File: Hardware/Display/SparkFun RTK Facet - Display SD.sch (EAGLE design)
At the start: 30 parts, among them J1 FPC_12_0.5MM_BACKFLIP, J2 MICRO-SD-PUSH-PUSH-EXT-PIN, J3 FPC_12_0.5MM_BACKFLIP, U13 LIS2DH12

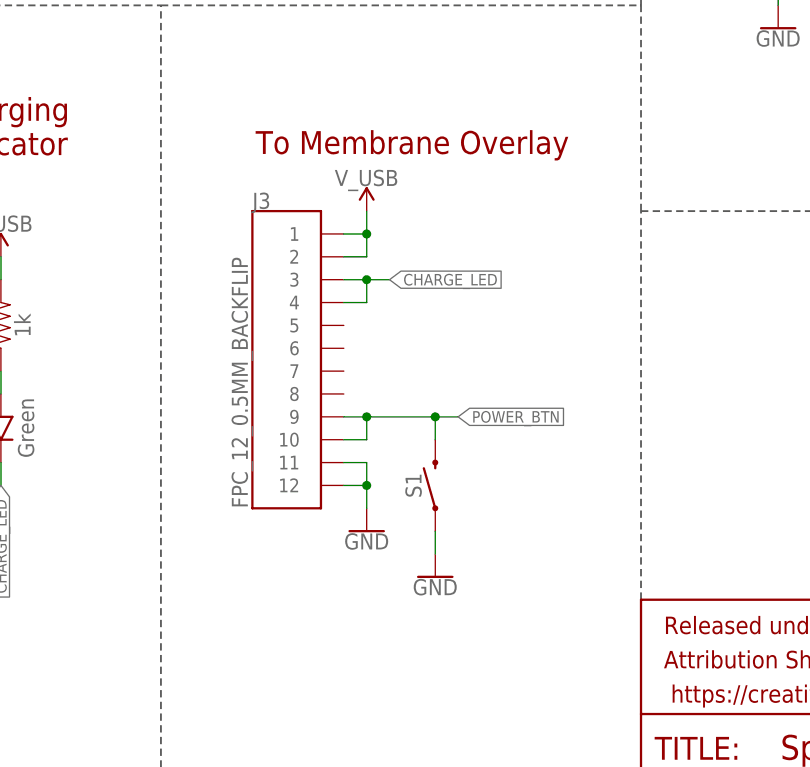
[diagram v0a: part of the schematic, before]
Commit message: Move to LIF overlay connector.
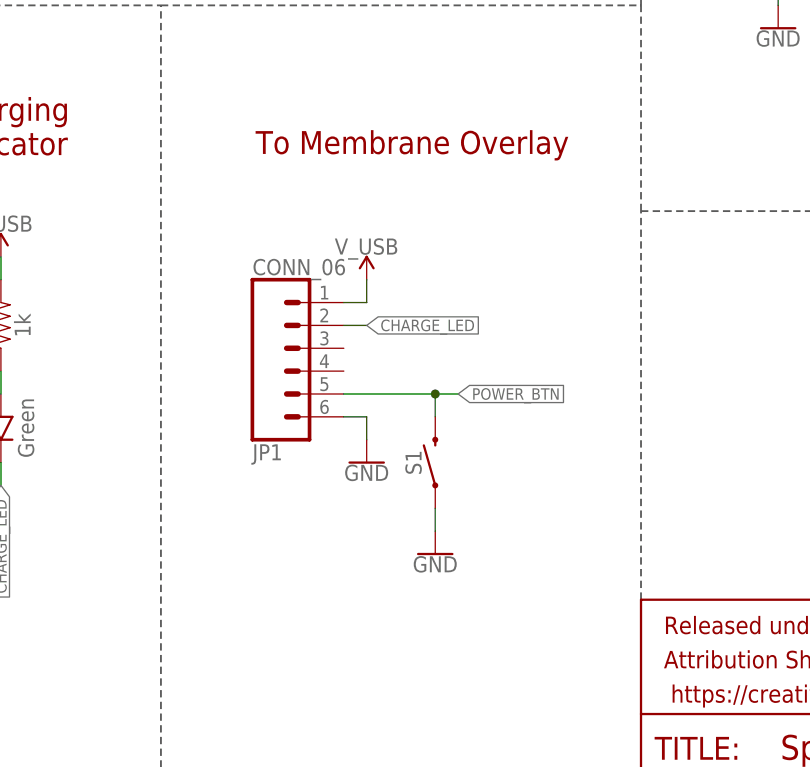
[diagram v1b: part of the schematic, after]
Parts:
- removed J3: FPC_12_0.5MM_BACKFLIP, RTK Facet:FPC_12_0.5MM_BACKFLIP
- added JP1: CONN_06, 1mm Pitch Connector:CONN_06
- LOGO5: value SFE_LOGO_NAME_FLAME.1_INCH -> SFE_LOGO_NAME_FLAME8_MM; device SparkFun-Aesthetics:SFE_LOGO_NAME_FLAME.1_INCH -> SparkFun-Aesthetics:SFE_LOGO_NAME_FLAME8_MM
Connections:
- net CHARGE_LED: now also JP1.2; no longer J3.3, J3.4
- net GND: now also JP1.6; no longer J3.11, J3.12
- net POWER_BTN: now also JP1.5; no longer J3.10, J3.9
- net V_USB: now also JP1.1; no longer J3.1, J3.2
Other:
- moved on the sheet: S1

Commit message: v15 panel files. Add tCream to LIF.
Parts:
- JP1: value CONN_06 -> (none); device 1mm Pitch Connector:CONN_06 -> SparkFun-Connectors:CONN_061MM-LIF
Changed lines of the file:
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@@
 <grid distance="0.1" unitdist="inch" unit="inch" style="lines" multiple="1" display="no" altdistance="0.01" altunitdist="inch" altunit="inch"/>
 <layers>
-<layer number="1" name="Top" color="4" fill="1" visible="yes" active="no"/>
-<layer number="2" name="Route2" color="1" fill="3" visible="yes" active="no"/>
-<layer number="3" name="Route3" color="4" fill="3" visible="yes" active="no"/>
-<layer number="4" name="Route4" color="1" fill="4" visible="yes" active="no"/>
-<layer number="5" name="Route5" color="4" fill="4" visible="yes" active="no"/>
-<layer number="6" name="Route6" color="1" fill="8" visible="yes" active="no"/>
-<layer number="7" name="Route7" color="4" fill="8" visible="yes" active="no"/>
-<layer number="8" name="Route8" color="1" fill="2" visible="yes" active="no"/>
-<layer number="9" name="Route9" color="4" fill="2" visible="yes" active="no"/>
-<layer number="10" name="Route10" color="1" fill="7" visible="yes" active="no"/>
-<layer number="11" name="Route11" color="4" fill="7" visible="yes" active="no"/>
-<layer number="12" name="Route12" color="1" fill="5" visible="yes" active="no"/>
-<layer number="13" name="Route13" color="4" fill="5" visible="yes" active="no"/>
-<layer number="14" name="Route14" color="1" fill="6" visible="yes" active="no"/>
-<layer number="15" name="Route15" color="4" fill="6" visible="yes" active="no"/>
-<layer number="16" name="Bottom" color="1" fill="1" visible="yes" active="no"/>
-<layer number="17" name="Pads" color="2" fill="1" visible="yes" active="no"/>
-<layer number="18" name="Vias" color="2" fill="1" visible="yes" active="no"/>
-<layer number="19" name="Unrouted" color="6" fill="1" visible="yes" active="no"/>
-<layer number="20" name="Dimension" color="24" fill="1" visible="yes" active="no"/>
-<layer number="21" name="tPlace" color="16" fill="1" visible="yes" active="no"/>
-<layer number="22" name="bPlace" color="14" fill="1" visible="yes" active="no"/>
-<layer number="23" name="tOrigins" color="15" fill="1" visible="yes" active="no"/>
-<layer number="24" name="bOrigins" color="15" fill="1" visible="yes" active="no"/>
-<layer number="25" name="tNames" color="7" fill="1" visible="yes" active="no"/>
-<layer number="26" name="bNames" color="7" fill="1" visible="yes" active="no"/>
-<layer number="27" name="tValues" color="7" fill="1" visible="yes" active="no"/>
-<layer number="28" name="bValues" color="7" fill="1" visible="yes" active="no"/>
+<layer number="1" name="Top" color="4" fill="1" visible="no" active="no"/>
+<layer number="2" name="Route2" color="1" fill="3" visible="no" active="no"/>
+<layer number="3" name="Route3" color="4" fill="3" visible="no" active="no"/>
+<layer number="4" name="Route4" color="1" fill="4" visible="no" active="no"/>
+<layer number="5" name="Route5" color="4" fill="4" visible="no" active="no"/>
+<layer number="6" name="Route6" color="1" fill="8" visible="no" active="no"/>
+<layer number="7" name="Route7" color="4" fill="8" visible="no" active="no"/>
+<layer number="8" name="Route8" color="1" fill="2" visible="no" active="no"/>
+<layer number="9" name="Route9" color="4" fill="2" visible="no" active="no"/>
+<layer number="10" name="Route10" color="1" fill="7" visible="no" active="no"/>
+<layer number="11" name="Route11" color="4" fill="7" visible="no" active="no"/>
+<layer number="12" name="Route12" color="1" fill="5" visible="no" active="no"/>
+<layer number="13" name="Route13" color="4" fill="5" visible="no" active="no"/>
+<layer number="14" name="Route14" color="1" fill="6" visible="no" active="no"/>
+<layer number="15" name="Route15" color="4" fill="6" visible="no" active="no"/>
+<layer number="16" name="Bottom" color="1" fill="1" visible="no" active="no"/>
+<layer number="17" name="Pads" color="2" fill="1" visible="no" active="no"/>
+<layer number="18" name="Vias" color="2" fill="1" visible="no" active="no"/>
+<layer number="19" name="Unrouted" color="6" fill="1" visible="no" active="no"/>
+<layer number="20" name="Dimension" color="24" fill="1" visible="no" active="no"/>
+<layer number="21" name="tPlace" color="16" fill="1" visible="no" active="no"/>
+<layer number="22" name="bPlace" color="14" fill="1" visible="no" active="no"/>
+<layer number="23" name="tOrigins" color="15" fill="1" visible="no" active="no"/>
+<layer number="24" name="bOrigins" color="15" fill="1" visible="no" active="no"/>
+<layer number="25" name="tNames" color="7" fill="1" visible="no" active="no"/>
+<layer number="26" name="bNames" color="7" fill="1" visible="no" active="no"/>
+<layer number="27" name="tValues" color="7" fill="1" visible="no" active="no"/>
+<layer number="28" name="bValues" color="7" fill="1" visible="no" active="no"/>
 <layer number="29" name="tStop" color="7" fill="3" visible="no" active="no"/>
 <layer number="30" name="bStop" color="7" fill="6" visible="no" active="no"/>
@@
 <layer number="35" name="tGlue" color="7" fill="4" visible="no" active="no"/>
 <layer number="36" name="bGlue" color="7" fill="5" visible="no" active="no"/>
-<layer number="37" name="tTest" color="7" fill="1" visible="yes" active="no"/>
-<layer number="38" name="bTest" color="7" fill="1" visible="yes" active="no"/>
+<layer number="37" name="tTest" color="7" fill="1" visible="no" active="no"/>
+<layer number="38" name="bTest" color="7" fill="1" visible="no" active="no"/>
 <layer number="39" name="tKeepout" color="4" fill="11" visible="no" active="no"/>
 <layer number="40" name="bKeepout" color="1" fill="11" visible="no" active="no"/>
@@
 <layer number="44" name="Drills" color="7" fill="1" visible="no" active="no"/>
 <layer number="45" name="Holes" color="7" fill="1" visible="no" active="no"/>
-<layer number="46" name="Milling" color="3" fill="1" visible="yes" active="no"/>
-<layer number="47" name="Measures" color="7" fill="1" visible="yes" active="no"/>
-<layer number="48" name="Document" color="7" fill="1" visible="yes" active="no"/>
-<layer number="49" name="Reference" color="7" fill="1" visible="yes" active="no"/>
-<layer number="50" name="dxf" color="7" fill="1" visible="yes" active="no"/>
-<layer number="51" name="tDocu" color="6" fill="1" visible="yes" active="no"/>
-<layer number="52" name="bDocu" color="7" fill="1" visible="yes" active="no"/>
-<layer number="53" name="tGND_GNDA" color="7" fill="1" visible="yes" active="no"/>
-<layer number="54" name="bGND_GNDA" color="7" fill="1" visible="yes" active="no"/>
-<layer number="56" name="wert" color="7" fill="1" visible="yes" active="no"/>
-<layer number="57" name="tCAD" color="7" fill="1" visible="yes" active="no"/>
-<layer number="58" name="bCAD" color="7" fill="1" visible="yes" active="no"/>
-<layer number="59" name="tCarbon" color="7" fill="1" visible="yes" active="no"/>
-<layer number="60" name="bCarbon" color="7" fill="1" visible="yes" active="no"/>
+<layer number="46" name="Milling" color="3" fill="1" visible="no" active="no"/>
+<layer number="47" name="Measures" color="7" fill="1" visible="no" active="no"/>
+<layer number="48" name="Document" color="7" fill="1" visible="no" active="no"/>
+<layer number="49" name="Reference" color="7" fill="1" visible="no" active="no"/>
+<layer number="50" name="dxf" color="7" fill="1" visible="no" active="no"/>
+<layer number="51" name="tDocu" color="6" fill="1" visible="no" active="no"/>
+<layer number="52" name="bDocu" color="7" fill="1" visible="no" active="no"/>
+<layer number="53" name="tGND_GNDA" color="7" fill="1" visible="no" active="no"/>
+<layer number="54" name="bGND_GNDA" color="7" fill="1" visible="no" active="no"/>
+<layer number="56" name="wert" color="7" fill="1" visible="no" active="no"/>
+<layer number="57" name="tCAD" color="7" fill="1" visible="no" active="no"/>
+<layer number="58" name="bCAD" color="7" fill="1" visible="no" active="no"/>
+<layer number="59" name="tCarbon" color="7" fill="1" visible="no" active="no"/>
+<layer number="60" name="bCarbon" color="7" fill="1" visible="no" active="no"/>
 <layer number="88" name="SimResults" color="9" fill="1" visible="yes" active="yes"/>
 <layer number="89" name="SimProbes" color="9" fill="1" visible="yes" active="yes"/>
@@
 <layer number="154" name="FabDoc2" color="7" fill="1" visible="yes" active="yes"/>
 <layer number="155" name="FabDoc3" color="7" fill="1" visible="yes" active="yes"/>
+<layer number="156" name="gesam-Maß" color="7" fill="1" visible="no" active="no"/>
+<layer number="157" name="FaceMchng" color="7" fill="1" visible="no" active="no"/>
+<layer number="158" name="FaceMMeas" color="7" fill="1" visible="no" active="no"/>
+<layer number="159" name="Geh-Bear2" color="7" fill="1" visible="no" active="no"/>
+<layer number="160" name="Topologie" color="7" fill="1" visible="no" active="no"/>
+<layer number="161" name="tomplace2" color="7" fill="1" visible="no" active="no"/>
 <layer number="166" name="AntennaArea" color="7" fill="1" visible="no" active="no"/>
 <layer number="168" name="4mmHeightArea" color="7" fill="1" visible="no" active="no"/>
@@
 <layer number="250" name="Descript" color="7" fill="1" visible="yes" active="yes"/>
 <layer number="251" name="SMDround" color="7" fill="1" visible="yes" active="yes"/>
+<layer number="252" name="BR-BS" color="7" fill="1" visible="no" active="no"/>
 <layer number="253" name="Extra" color="7" fill="1" visible="no" active="no"/>
 <layer number="254" name="cooling" color="7" fill="1" visible="yes" active="yes"/>
@@
 <part name="SUPPLY11" library="SparkFun-PowerSymbols" deviceset="V_USB" device=""/>
 <part name="J2" library="SparkFun-Connectors" deviceset="MICRO-SD" device="-PUSH-PUSH-EXT-PIN"/>
-<part name="JP1" library="1mm Pitch Connector" deviceset="CONN_06" device=""/>
+<part name="JP1" library="SparkFun-Connectors" deviceset="CONN_06" device="1MM-LIF"/>
 <part name="SUPPLY9" library="SparkFun-PowerSymbols" deviceset="V_USB" device=""/>
 <part name="GND7" library="SparkFun-PowerSymbols" deviceset="GND" device=""/>

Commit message: Add I2C addresses to schematics
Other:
- note added: "7-Bit unshifted I²C address: 0x19"
- note added: "7-Bit unshifted I²C address: 0x3D"
- note removed: "7-Bit unshifted I2C address: 0x19"
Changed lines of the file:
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@@
 permanent I2C mode.</text>
 <text x="198.12" y="177.8" size="2.54" layer="94" align="center">microSD</text>
-<text x="200.66" y="86.36" size="1.778" layer="97" align="center">7-Bit unshifted I2C address: 0x19</text>
+<text x="200.66" y="86.36" size="1.778" layer="97" align="center">7-Bit unshifted I²C address: 0x19</text>
 <text x="198.12" y="129.54" size="2.54" layer="94" font="vector" align="center">LIS2DH12 / Accelerometer</text>
 <text x="121.92" y="86.36" size="2.54" layer="94" rot="MR180" align="center">To Membrane Overlay</text>
@@
 Indicator</text>
 <text x="171.196" y="11.43" size="2.54" layer="94" font="vector">N. Seidle</text>
+<text x="114.3" y="106.68" size="1.778" layer="97" align="center">7-Bit unshifted I²C address: 0x3D</text>
 </plain>
 <instances>

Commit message: Add I2C test header to display board - v1.6
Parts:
- added J3: (no value), SparkFun-Connectors:I2C_STANDARD_NO_SILK
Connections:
- net 3.3V: now also J3.2
- net ESP_21/SDA: now also J3.3
- net ESP_22/SCL: now also J3.4
- net GND: now also J3.1

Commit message: Remove silk from around the accel FP for DFM.
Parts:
- U13: value LIS2DH12 -> LIS2DH12NS; device SparkFun-Sensors:LIS2DH12 -> SparkFun-Sensors:LIS2DH12NS
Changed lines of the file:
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@@
 <part name="C7" library="SparkFun-Capacitors" deviceset="1.0UF" device="-0603-16V-10%" value="1.0uF"/>
 <part name="R2" library="SparkFun-Resistors" deviceset="10KOHM" device="-0603-1/10W-1%" value="10k"/>
-<part name="JP3" library="SparkFun-Jumpers" deviceset="JUMPER-SMT_2_NO" device="_SILK" package3d_urn="urn:adsk.eagle:package:39279/1" value=""/>
+<part name="JP3" library="SparkFun-Jumpers" deviceset="JUMPER-SMT_2_NO" device="_SILK" package3d_urn="urn:adsk.eagle:package:39279/1" value="JUMPER-SMT_2_NO_SILK"/>
 <part name="FID3" library="SparkFun-Aesthetics" deviceset="FIDUCIAL" device="1X2"/>
 <part name="FID4" library="SparkFun-Aesthetics" deviceset="FIDUCIAL" device="1X2"/>
@@
 <part name="GND2" library="SparkFun-PowerSymbols" deviceset="GND" device=""/>
 <part name="J1" library="RTK Facet" deviceset="FPC_12_0.5MM" device="_BACKFLIP" value="FPC_12_0.5MM_BACKFLIP"/>
-<part name="U13" library="SparkFun-Sensors" deviceset="LIS2DH12" device=""/>
+<part name="U13" library="SparkFun-Sensors" deviceset="LIS2DH12" device="NS" value="LIS2DH12NS"/>
 <part name="GND4" library="SparkFun-PowerSymbols" deviceset="GND" device=""/>
 <part name="GND1" library="SparkFun-PowerSymbols" deviceset="GND" device=""/>
@@
 <attribute name="VALUE" x="19.558" y="43.434" size="1.778" layer="96" rot="R90"/>
 </instance>
-<instance part="U13" gate="G$1" x="200.66" y="106.68" smashed="yes">
+<instance part="U13" gate="U1" x="200.66" y="106.68" smashed="yes">
 <attribute name="NAME" x="190.5" y="119.634" size="1.778" layer="95"/>
 <attribute name="VALUE" x="190.5" y="94.234" size="1.778" layer="96" rot="MR180" align="top-left"/>
@@
 </segment>
 <segment>
-<pinref part="U13" gate="G$1" pin="GND"/>
+<pinref part="U13" gate="U1" pin="GND"/>
 <pinref part="GND4" gate="1" pin="GND"/>
 <wire x1="187.96" y1="99.06" x2="185.42" y2="99.06" width="0.1524" layer="91"/>
 <wire x1="185.42" y1="99.06" x2="185.42" y2="96.52" width="0.1524" layer="91"/>
-<pinref part="U13" gate="G$1" pin="RES"/>
+<pinref part="U13" gate="U1" pin="RES"/>
 <wire x1="187.96" y1="104.14" x2="185.42" y2="104.14" width="0.1524" layer="91"/>
 <wire x1="185.42" y1="104.14" x2="185.42" y2="99.06" width="0.1524" layer="91"/>
@@
 </segment>
 <segment>
-<pinref part="U13" gate="G$1" pin="VDD_IO"/>
+<pinref part="U13" gate="U1" pin="VDD_IO"/>
 <wire x1="187.96" y1="116.84" x2="185.42" y2="116.84" width="0.1524" layer="91"/>
-<pinref part="U13" gate="G$1" pin="VDD"/>
+<pinref part="U13" gate="U1" pin="VDD"/>
 <wire x1="187.96" y1="114.3" x2="185.42" y2="114.3" width="0.1524" layer="91"/>
 <wire x1="185.42" y1="114.3" x2="185.42" y2="116.84" width="0.1524" layer="91"/>
@@
 </segment>
 <segment>
-<pinref part="U13" gate="G$1" pin="CS"/>
+<pinref part="U13" gate="U1" pin="CS"/>
 <wire x1="213.36" y1="116.84" x2="215.9" y2="116.84" width="0.1524" layer="91"/>
 <wire x1="215.9" y1="116.84" x2="215.9" y2="119.38" width="0.1524" layer="91"/>
 <junction x="215.9" y="116.84"/>
 <wire x1="215.9" y1="116.84" x2="215.9" y2="114.3" width="0.1524" layer="91"/>
-<pinref part="U13" gate="G$1" pin="SDO/SA0"/>
+<pinref part="U13" gate="U1" pin="SDO/SA0"/>
 <wire x1="213.36" y1="114.3" x2="215.9" y2="114.3" width="0.1524" layer="91"/>
 <pinref part="SUPPLY8" gate="G$1" pin="3.3V"/>
@@
 <net name="ESP_22/SCL" class="0">
 <segment>
-<pinref part="U13" gate="G$1" pin="SCL/SPC"/>
+<pinref part="U13" gate="U1" pin="SCL/SPC"/>
 <wire x1="213.36" y1="111.76" x2="215.9" y2="111.76" width="0.1524" layer="91"/>
 <label x="215.9" y="111.76" size="1.27" layer="95" xref="yes"/>
@@
 <net name="ESP_21/SDA" class="0">
 <segment>
-<pinref part="U13" gate="G$1" pin="SDA/SDI/SDO"/>
+<pinref part="U13" gate="U1" pin="SDA/SDI/SDO"/>
 <wire x1="213.36" y1="109.22" x2="215.9" y2="109.22" width="0.1524" layer="91"/>
 <label x="215.9" y="109.22" size="1.27" layer="95" xref="yes"/>

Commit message: Convert connector and display boards to KiCad
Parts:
- OLED1: value OLED0.66 -> OLED0.66-TRIMTRIM; device SparkFun-Displays:OLED0.66 -> SparkFun-Displays:OLED0.66-TRIMTRIM
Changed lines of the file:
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@@
 </classes>
 <parts>
-<part name="OLED1" library="SparkFun-Displays" deviceset="OLED0.66" device=""/>
+<part name="OLED1" library="SparkFun-Displays" deviceset="OLED0.66-TRIM" device="TRIM"/>
 <part name="FRAME1" library="SparkFun-Aesthetics" deviceset="FRAME-LETTER" device=""/>
 <part name="C1" library="SparkFun-Capacitors" deviceset="2.2UF" device="-0805-25V-(+80/-20%)" value="2.2uF"/>
@@
 <attribute name="VALUE" x="193.04" y="139.7" size="1.778" layer="96"/>
 </instance>
-<instance part="JP1" gate="JP1" x="109.22" y="63.5" smashed="yes" rot="MR180">
+<instance part="JP1" gate="J1" x="109.22" y="63.5" smashed="yes" rot="MR180">
 <attribute name="VALUE" x="104.14" y="73.406" size="1.778" layer="96" font="vector" rot="MR180"/>
 <attribute name="NAME" x="104.14" y="52.832" size="1.778" layer="95" font="vector" rot="MR180"/>
@@
 </segment>
 <segment>
-<pinref part="JP1" gate="JP1" pin="6"/>
+<pinref part="JP1" gate="J1" pin="6"/>
 <wire x1="114.3" y1="55.88" x2="116.84" y2="55.88" width="0.1524" layer="91"/>
 <wire x1="116.84" y1="55.88" x2="116.84" y2="53.34" width="0.1524" layer="91"/>
@@
 </segment>
 <segment>
-<pinref part="JP1" gate="JP1" pin="2"/>
+<pinref part="JP1" gate="J1" pin="2"/>
 <wire x1="114.3" y1="66.04" x2="116.84" y2="66.04" width="0.1524" layer="91"/>
 <label x="116.84" y="66.04" size="1.27" layer="95" xref="yes"/>
@@
 </segment>
 <segment>
-<pinref part="JP1" gate="JP1" pin="5"/>
+<pinref part="JP1" gate="J1" pin="5"/>
 <wire x1="114.3" y1="58.42" x2="124.46" y2="58.42" width="0.1524" layer="91"/>
 <label x="127" y="58.42" size="1.27" layer="95" xref="yes"/>
@@
 </segment>
 <segment>
-<pinref part="JP1" gate="JP1" pin="1"/>
+<pinref part="JP1" gate="J1" pin="1"/>
 <wire x1="114.3" y1="68.58" x2="116.84" y2="68.58" width="0.1524" layer="91"/>
 <wire x1="116.84" y1="68.58" x2="116.84" y2="71.12" width="0.1524" layer="91"/>
